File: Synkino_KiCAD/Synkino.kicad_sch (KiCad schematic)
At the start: 162 parts, among them J1 Pwr, J10 EYE8_OUT, J11 EYE4_OUT, J12 2.5mm, J13 EYE5_OUT, J2 2.5mm, J3 3.5mm, J4 Micro_SD_Card_Det_Hirose_DM3AT, J5 EYE1_OUT, J6 EYE6_OUT, J7 EYE2_OUT, J8 EYE7_OUT, J9 EYE3_OUT, Q1 IRF7319, Q2 BC847, Q3 IRLML2244, SW1 SW_Push, SW2 Rotary_Encoder_Switch, SW3 SW_Push, U1 MCP1702T-5002E/MB, U10 ATMEGA328P-AU, U11 QRE1113, U12 QRE1113, U13 QRE1113, U14 QRE1113, U15 QRE1113, U16 QRE1113, U17 24LC256, U18 QRE1113, U2 ATMEGA328P-AU, U3 74HC4050, U4 SPIOLED128x64, U5 AP7312-1833W6-7, U6 74HC14, U7 VS1053B, U8 MAX4741, U9 QRE1113, X1 FTDIconn, X2 ICSP, X3 FTDIconn, X4 ICSP, Y1 16Mhz, Y2 12.288MHz, Y3 16Mhz

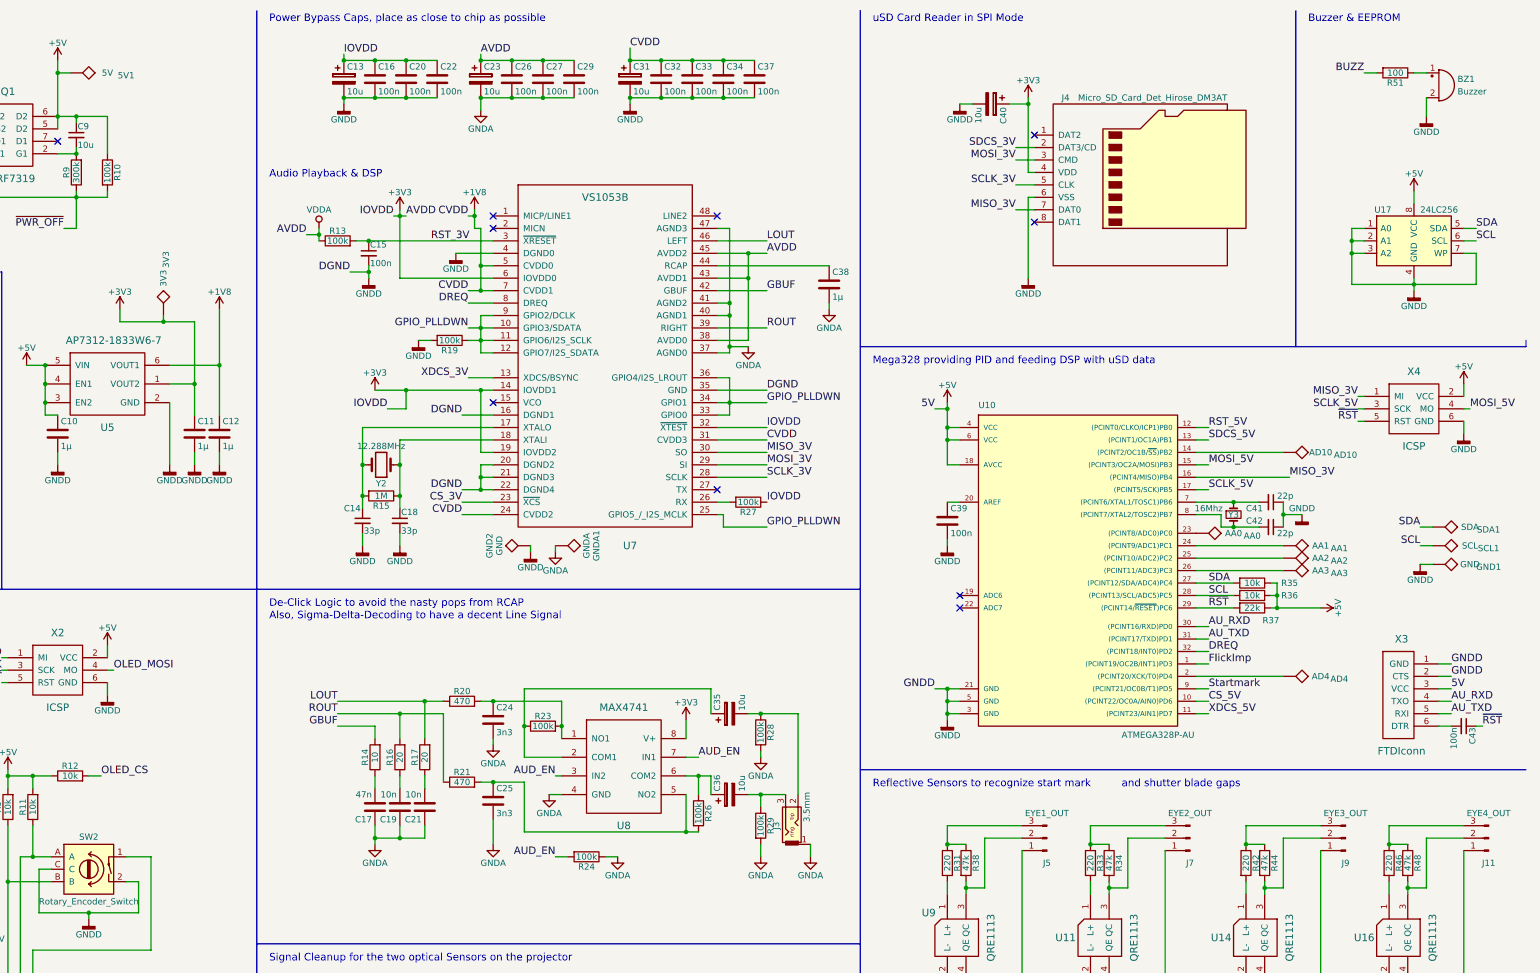
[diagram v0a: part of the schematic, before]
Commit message: Bul Footprint change for SMTA
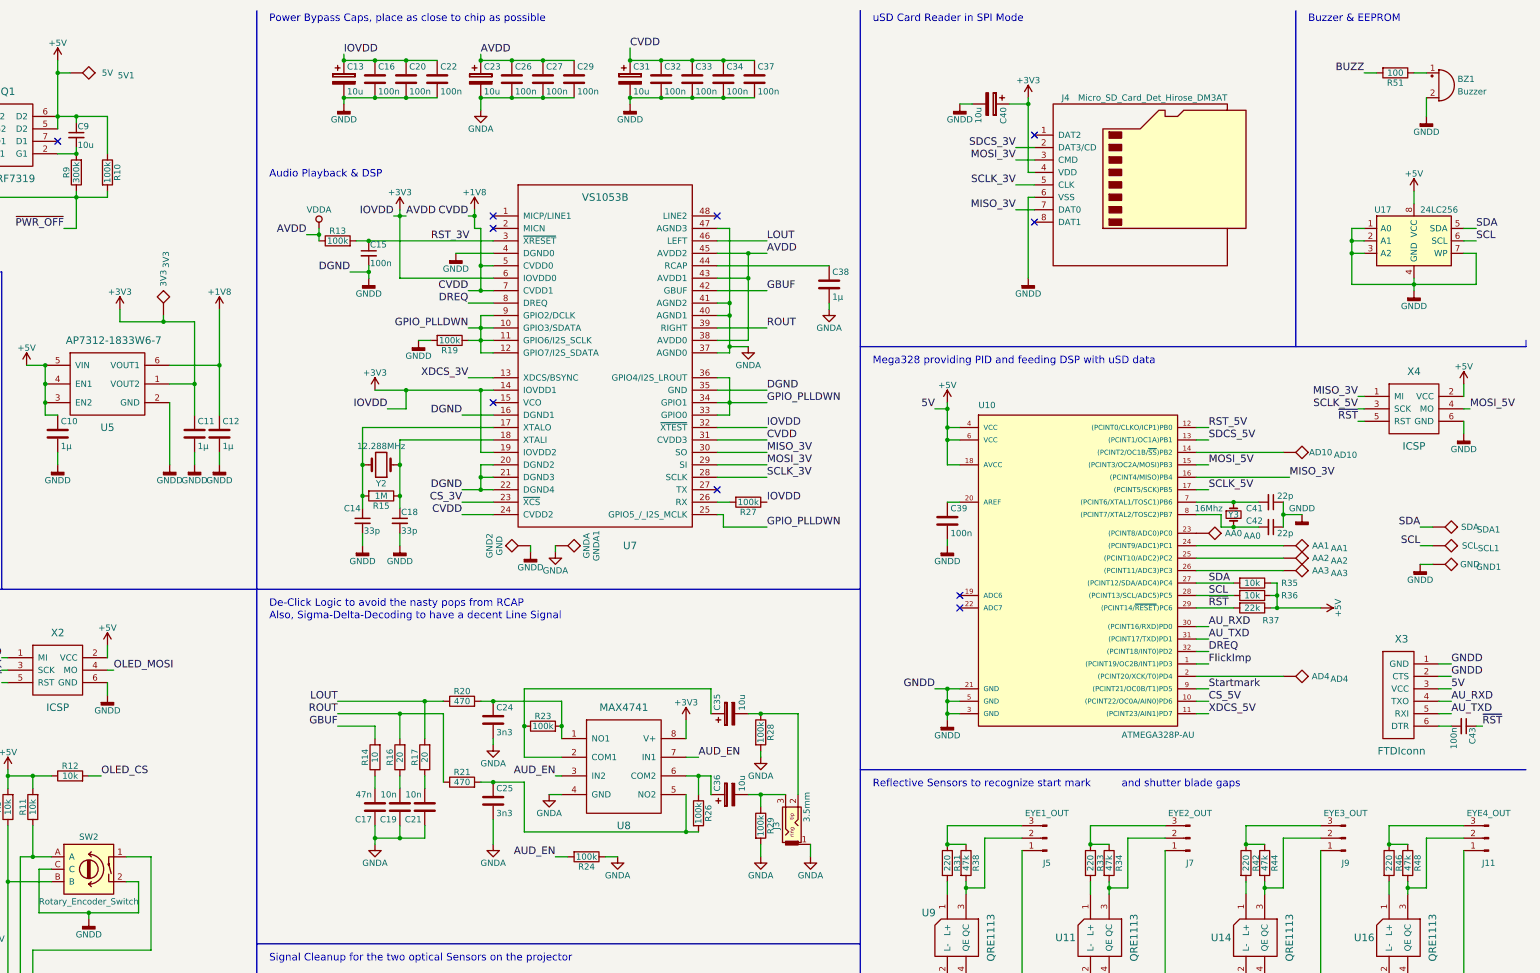
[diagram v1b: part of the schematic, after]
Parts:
- C13, C23, C31, C35, C36, C40: footprint Capacitors_SMD:CP_Elec_4x5.8 -> Capacitor_SMD:CP_Elec_4x5.8
- D2, D3: footprint LEDs:LED_0805_HandSoldering -> LED_SMD:LED_0805_2012Metric
- Q2: footprint TO_SOT_Packages_SMD:SOT-23_Handsoldering -> Package_TO_SOT_SMD:SOT-23
- Q3: footprint TO_SOT_Packages_SMD:SOT-23 -> Package_TO_SOT_SMD:SOT-23
- R1, R10, R11, R12, R13, R14, R15, R16, R17, R18, R19, R2, R20, R21, R22, R23, R24, R25, R26, R27, R28, R29, R3, R30, R31, R32, R33, R34, R35, R36, R37, R38, R39, R4, R40, R41, R42, R43, R44, R45, R46, R47, R48, R49, R5, R50, R51, R52, R53, R6, R7, R8, R9: footprint Resistors_SMD:R_0805_HandSoldering -> Resistor_SMD:R_0805_2012Metric

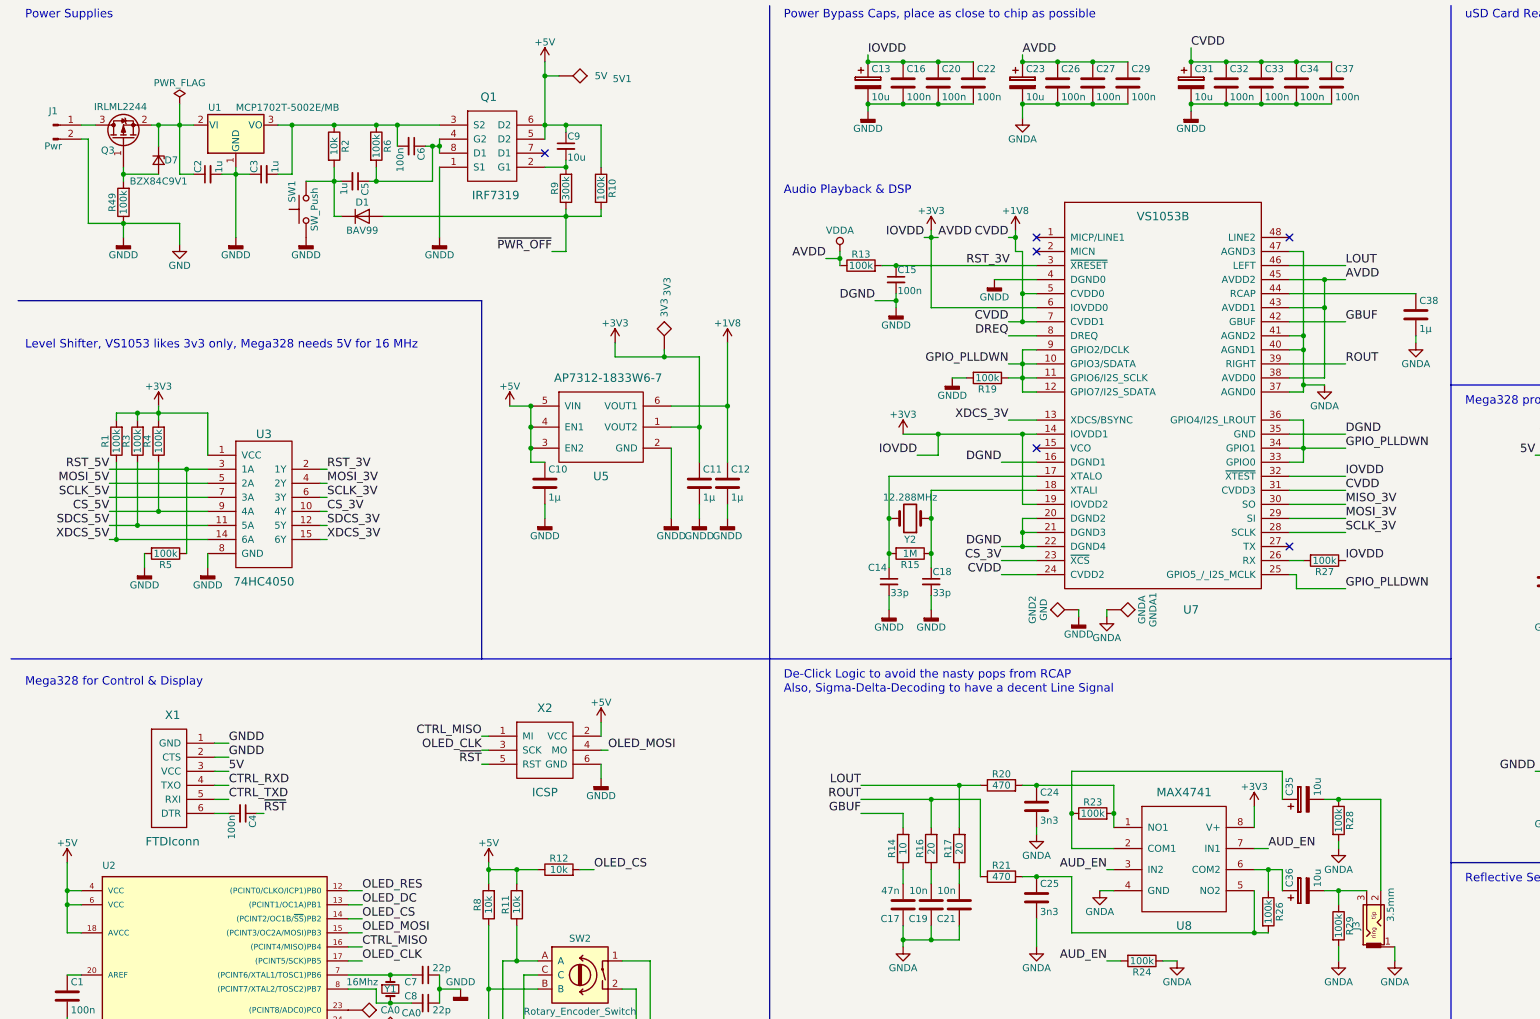
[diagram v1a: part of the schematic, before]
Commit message: Optimizing for SMTA (and sanity)
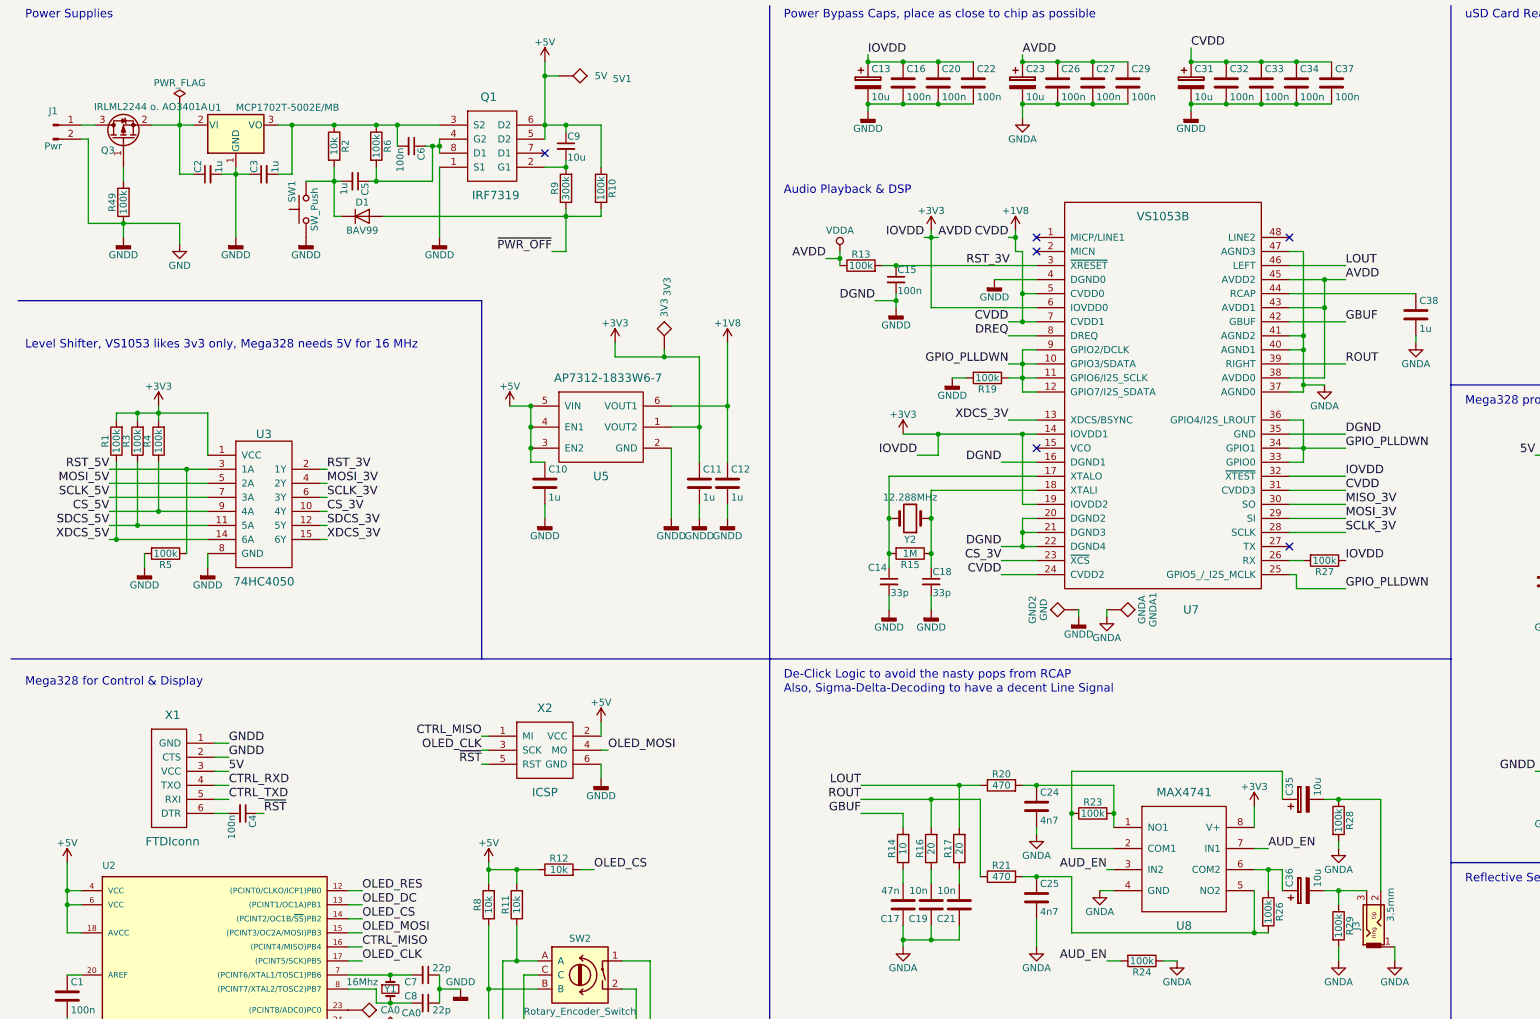
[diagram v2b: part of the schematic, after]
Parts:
- removed D7: BZX84C9V1, lib_fp:D_SOT-23_1A3K, symbol Synkino-rescue:D_Zener_Small
- C1, C15, C16, C20, C22, C26, C27, C28, C29, C30, C32, C33, C34, C37, C39, C4, C43, C6: Inventory (none) -> B; LCSC (none) -> C49678
- C10, C11, C12, C38: value 1µ -> 1u; Inventory (none) -> B; LCSC (none) -> C28323
- C13, C23, C31, C35, C36, C40: Inventory (none) -> E; LCSC (none) -> C249817
- C14, C18, C41, C42, C7, C8: Inventory (none) -> B; LCSC (none) -> C1804
- C17: Inventory (none) -> B; LCSC (none) -> C53134
- C19, C21: Inventory (none) -> B; LCSC (none) -> C1710
- C2, C3, C5: Inventory (none) -> B; LCSC (none) -> C28323
- C24, C25: value 3n3 -> 4n7; Inventory (none) -> B; LCSC (none) -> C1744
- C9: Inventory (none) -> B; LCSC (none) -> C15850
- D1: Inventory (none) -> B; LCSC (none) -> C2500
- D2, D3: Inventory (none) -> B; LCSC (none) -> C84256
- Q3: value IRLML2244 -> IRLML2244 o. AO3401A; Inventory (none) -> B; LCSC (none) -> C15127
